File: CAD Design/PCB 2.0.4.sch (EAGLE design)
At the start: 53 parts, among them U1 CC2538, U2 MAX1555, X1 32MHz, X2 FC-12M

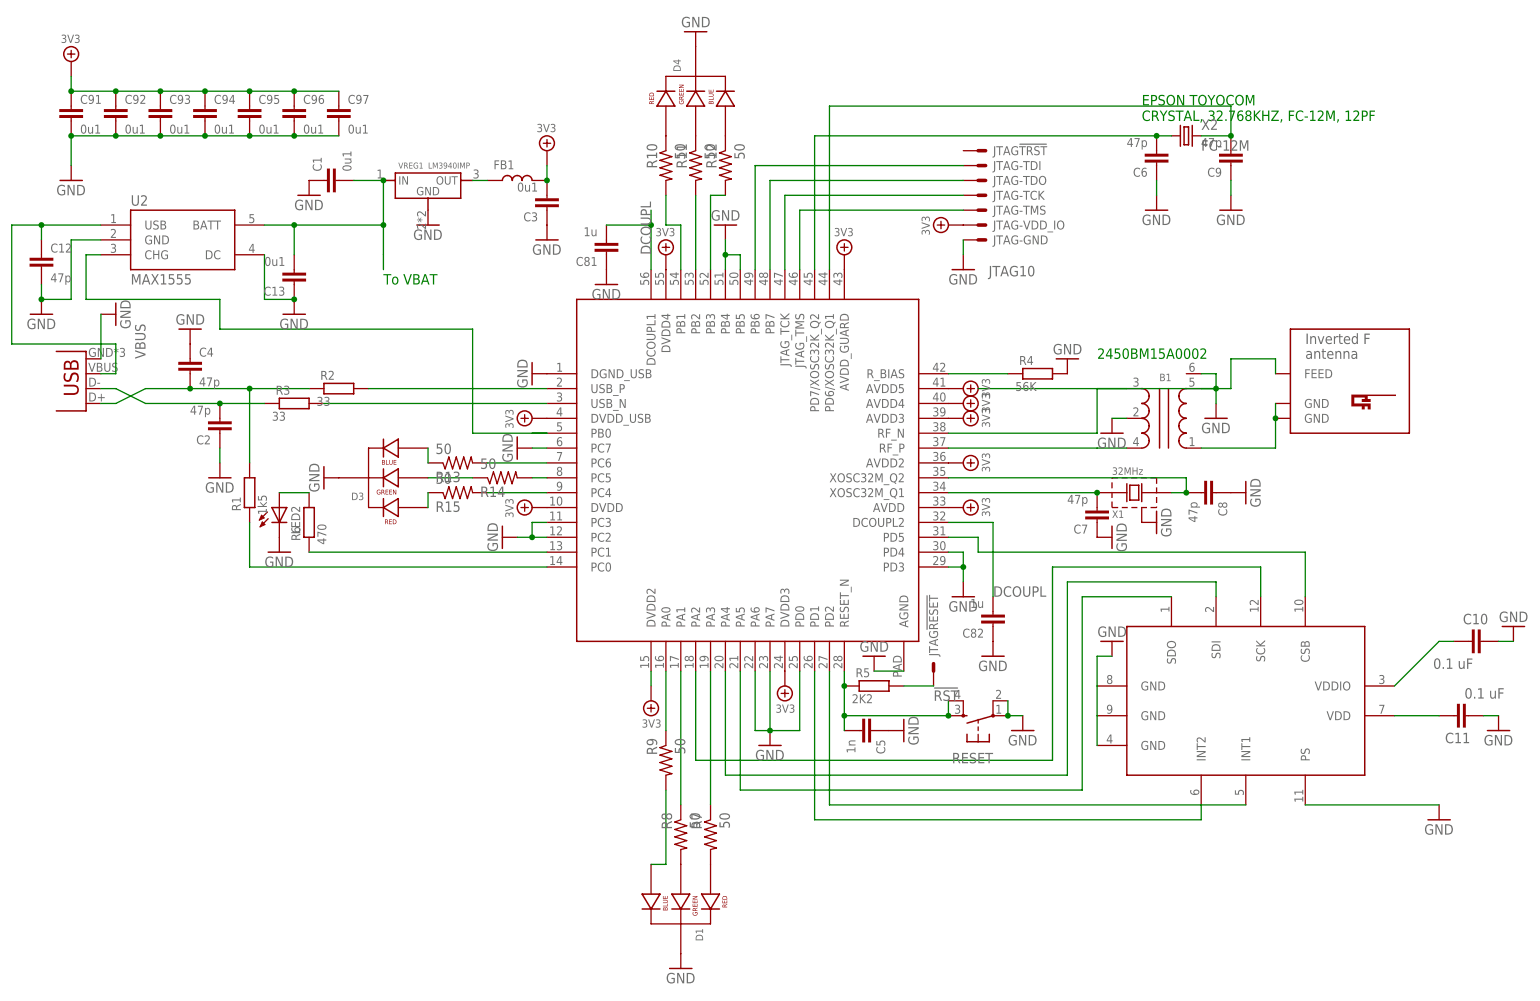
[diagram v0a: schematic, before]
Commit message: Updated resistor values
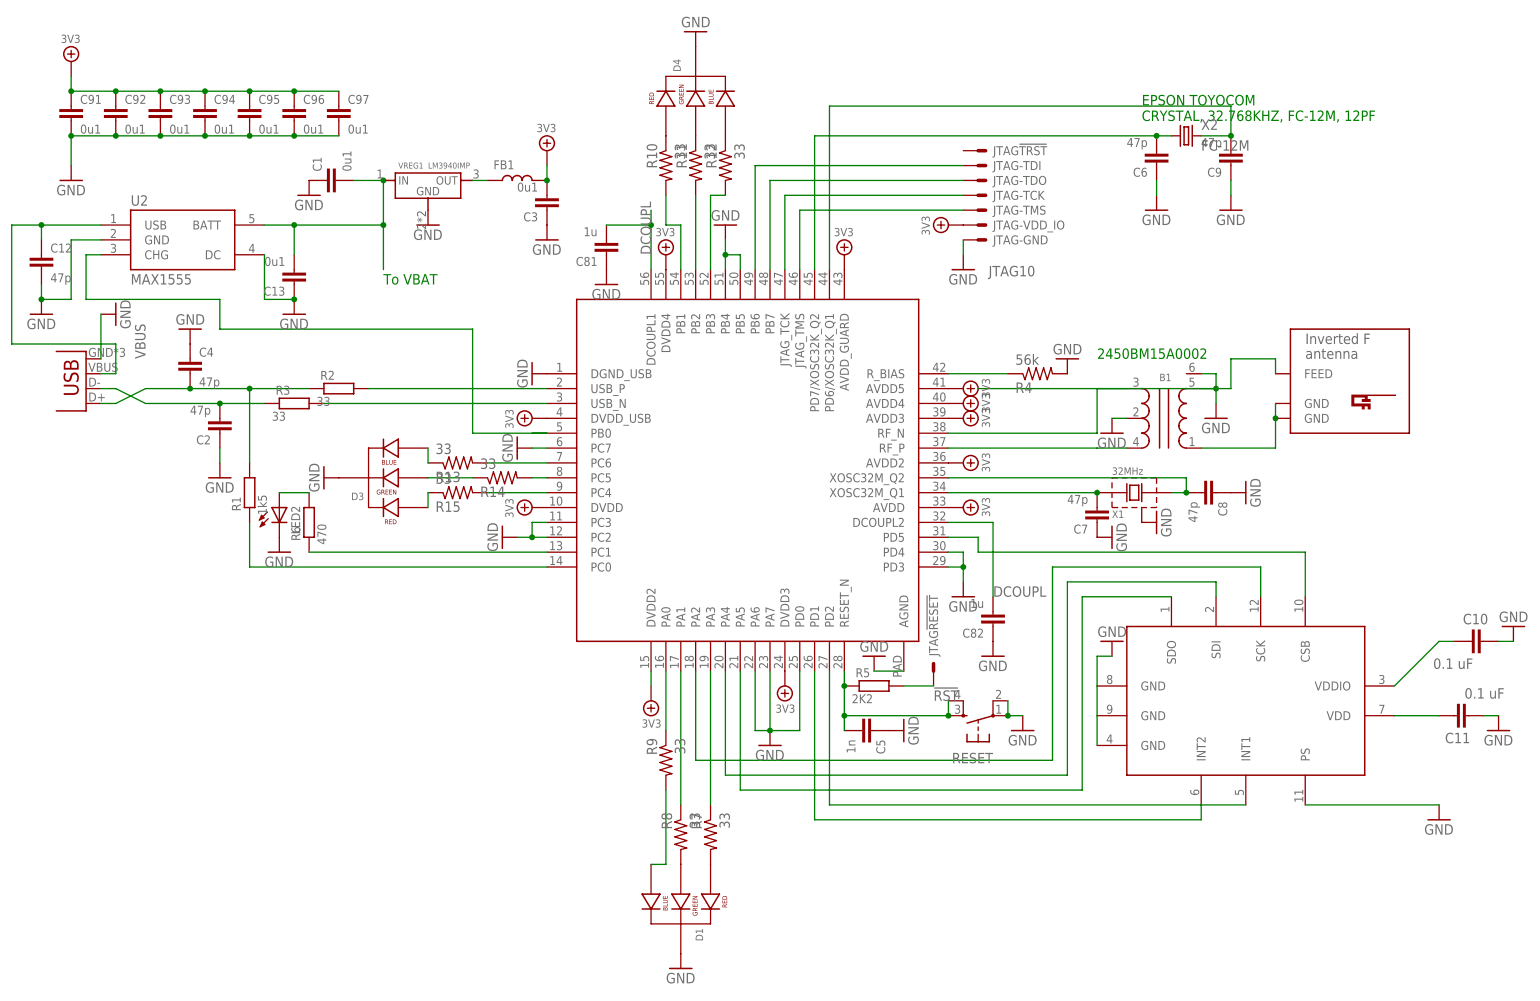
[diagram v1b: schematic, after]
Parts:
- R10, R11, R12, R13, R14, R15, R7, R8, R9: value 50 -> 33
- R4: value 56K -> 56k; device discrete:RR603 -> rcl:R-US_R0402
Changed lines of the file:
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@@
 <part name="3V3_PWR10" library="supply" deviceset="3V3" device=""/>
 <part name="3V3_PWR11" library="supply" deviceset="3V3" device=""/>
-<part name="R4" library="discrete" deviceset="R" device="R603" value="56K"/>
 <part name="GND6" library="supply1" deviceset="GND" device=""/>
 <part name="GND5" library="supply1" deviceset="GND" device=""/>
@@
 <part name="D3" library="SparkFun-LED" deviceset="LED-RGB-CC-THRU" device="CLEAR"/>
 <part name="GND38" library="supply1" deviceset="GND" device=""/>
-<part name="R7" library="rcl" deviceset="R-US_" device="R0402" value="50"/>
-<part name="R8" library="rcl" deviceset="R-US_" device="R0402" value="50"/>
-<part name="R9" library="rcl" deviceset="R-US_" device="R0402" value="50"/>
-<part name="R10" library="rcl" deviceset="R-US_" device="R0402" value="50"/>
-<part name="R11" library="rcl" deviceset="R-US_" device="R0402" value="50"/>
-<part name="R12" library="rcl" deviceset="R-US_" device="R0402" value="50"/>
-<part name="R13" library="rcl" deviceset="R-US_" device="R0402" value="50"/>
-<part name="R14" library="rcl" deviceset="R-US_" device="R0402" value="50"/>
-<part name="R15" library="rcl" deviceset="R-US_" device="R0402" value="50"/>
+<part name="R7" library="rcl" deviceset="R-US_" device="R0402" value="33"/>
+<part name="R8" library="rcl" deviceset="R-US_" device="R0402" value="33"/>
+<part name="R9" library="rcl" deviceset="R-US_" device="R0402" value="33"/>
+<part name="R10" library="rcl" deviceset="R-US_" device="R0402" value="33"/>
+<part name="R11" library="rcl" deviceset="R-US_" device="R0402" value="33"/>
+<part name="R12" library="rcl" deviceset="R-US_" device="R0402" value="33"/>
+<part name="R13" library="rcl" deviceset="R-US_" device="R0402" value="33"/>
+<part name="R14" library="rcl" deviceset="R-US_" device="R0402" value="33"/>
+<part name="R15" library="rcl" deviceset="R-US_" device="R0402" value="33"/>
+<part name="R4" library="rcl" deviceset="R-US_" device="R0402" value="56k"/>
 </parts>
 <sheets>
@@
 <instance part="3V3_PWR10" gate="A" x="167.64" y="109.22" rot="R270"/>
 <instance part="3V3_PWR11" gate="A" x="167.64" y="111.76" rot="R270"/>
-<instance part="R4" gate="G$1" x="180.34" y="114.3"/>
 <instance part="GND6" gate="1" x="185.42" y="116.84" rot="R180"/>
 <instance part="GND5" gate="1" x="152.4" y="66.04" rot="R180"/>
@@
 <instance part="R14" gate="G$1" x="88.9" y="96.52" rot="MR180"/>
 <instance part="R15" gate="G$1" x="81.28" y="93.98" rot="MR180"/>
+<instance part="R4" gate="G$1" x="180.34" y="114.3" rot="MR180"/>
 </instances>
 <busses>
@@
 <pinref part="C4" gate="C" pin="1"/>
 <pinref part="GND2" gate="1" pin="GND"/>
-</segment>
-<segment>
-<pinref part="R4" gate="G$1" pin="2"/>
-<pinref part="GND6" gate="1" pin="GND"/>
 </segment>
 <segment>
@@
 <pinref part="GND38" gate="1" pin="GND"/>
 </segment>
+<segment>
+<pinref part="GND6" gate="1" pin="GND"/>
+<pinref part="R4" gate="G$1" pin="2"/>
+</segment>
 </net>
 <net name="3V3" class="0">
@@
 <segment>
 <pinref part="U1" gate="G$1" pin="R_BIAS"/>
+<wire x1="175.26" y1="114.3" x2="165.1" y2="114.3" width="0.1524" layer="91"/>
 <pinref part="R4" gate="G$1" pin="1"/>
-<wire x1="175.26" y1="114.3" x2="165.1" y2="114.3" width="0.1524" layer="91"/>
-</segment>
-</net>
+</segment>
+</net>
